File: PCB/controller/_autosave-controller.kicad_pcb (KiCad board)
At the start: 2 copper layers, 79 x 33 mm, 32 parts, among them J1 USB_C_Receptacle_USB2.0_16P, Q5 BSS138, SW2 SW_Push, SW3 SW_Push, U1 NanoS3, U2 COM-09032, U3 TPS61200DRC

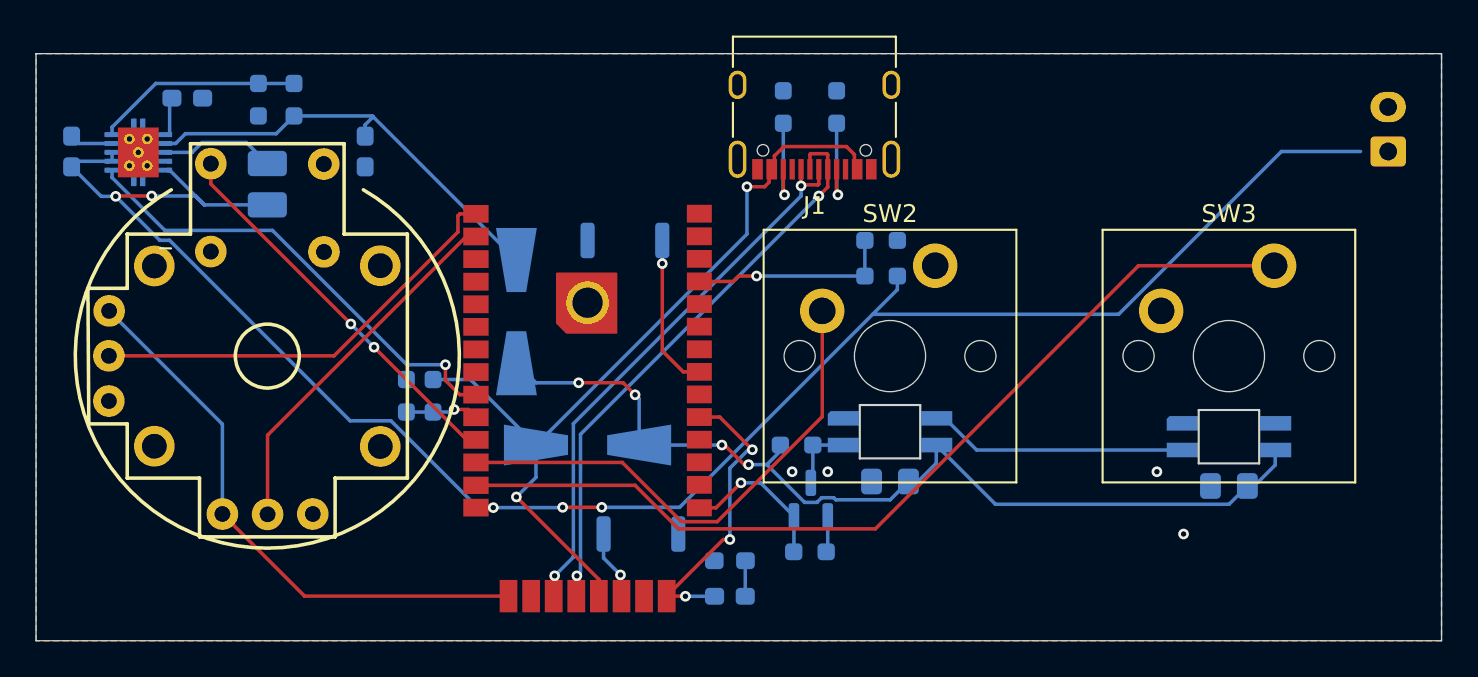
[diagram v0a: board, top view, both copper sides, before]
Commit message: Add production files for PCB controller design
- Created designators.csv with component designators and their counts.
- Added netlist.ipc containing detailed netlist information for PCB connections.
- Introduced positions.csv to specify component positions, rotations, and layers on the PCB.
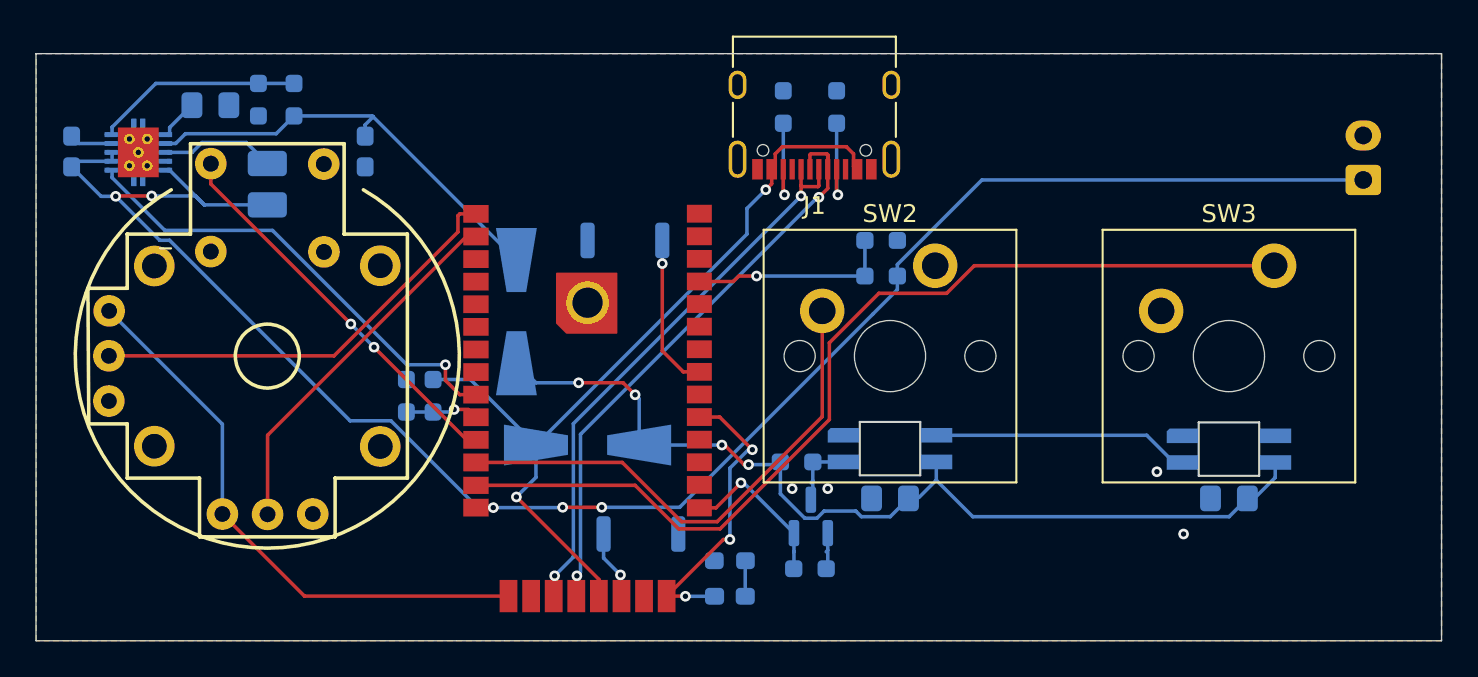
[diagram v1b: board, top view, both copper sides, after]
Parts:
- C1, C2: value C -> 0.1uF
- C5: footprint Capacitor_SMD:C_0603_1608Metric_Pad1.08x0.95mm_HandSolder -> Capacitor_SMD:C_0805_2012Metric_Pad1.18x1.45mm_HandSolder
- R1, R2: value R5.1kΩ -> R5.1k
- R3: value 120Ω -> 120
- R6: value 10kΩ -> 10k
- R7: value 15kΩ -> 15k
- R8, R9: value 100kΩ -> 100k
- moved BT1 2.13 mm to (201.6, 24.1)
- moved C5 1.36 mm to (136.8, 19.9)
- moved C1 0.95 mm to (175.0, 42.0)
- moved D2 0.95 mm to (175.0, 39.2)
- moved Q5 0.95 mm to (170.6, 43.0)
- moved R4 0.95 mm to (170.5, 46.0)
- moved R5 0.95 mm to (169.8, 40.0)
- moved C2 0.70 mm to (194.1, 42.0)
- moved D3 0.70 mm to (194.1, 39.2)
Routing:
- net USE: track 52.0 -> 54.5 mm
- net VBAT: track 106.0 -> 103.6 mm
- net D-: track 32.2 -> 33.2 mm
- net VBUS: track 54.0 -> 53.1 mm
- net +5V: track 46.5 -> 45.9 mm
